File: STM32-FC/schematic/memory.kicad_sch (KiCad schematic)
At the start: 6 parts, among them J4 TF-06A, U6 W25X40CLUXIG

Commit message: v2.0.0 beta init
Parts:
- J4: footprint TF-06A:TF06A -> TF06A
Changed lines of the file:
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@@
 			)
 		)
-		(property "Footprint" "TF-06A:TF06A"
+		(property "Footprint" "TF06A"
 			(at 177.8 127.94 0)
 			(effects

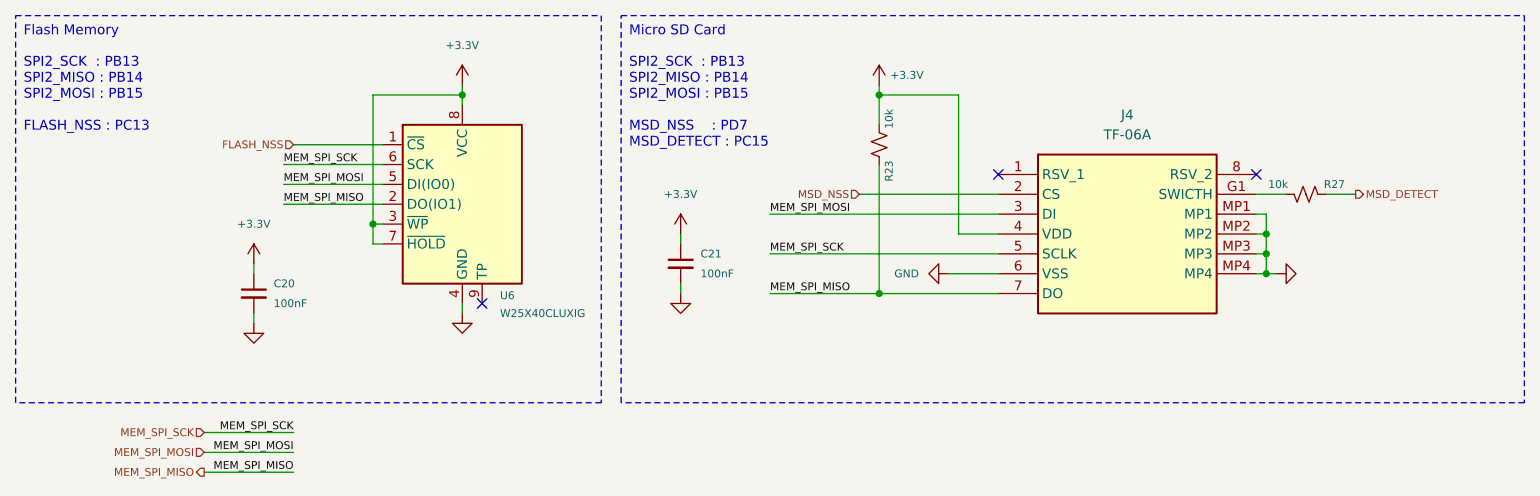
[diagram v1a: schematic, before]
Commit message: add basic circuit stm32f7
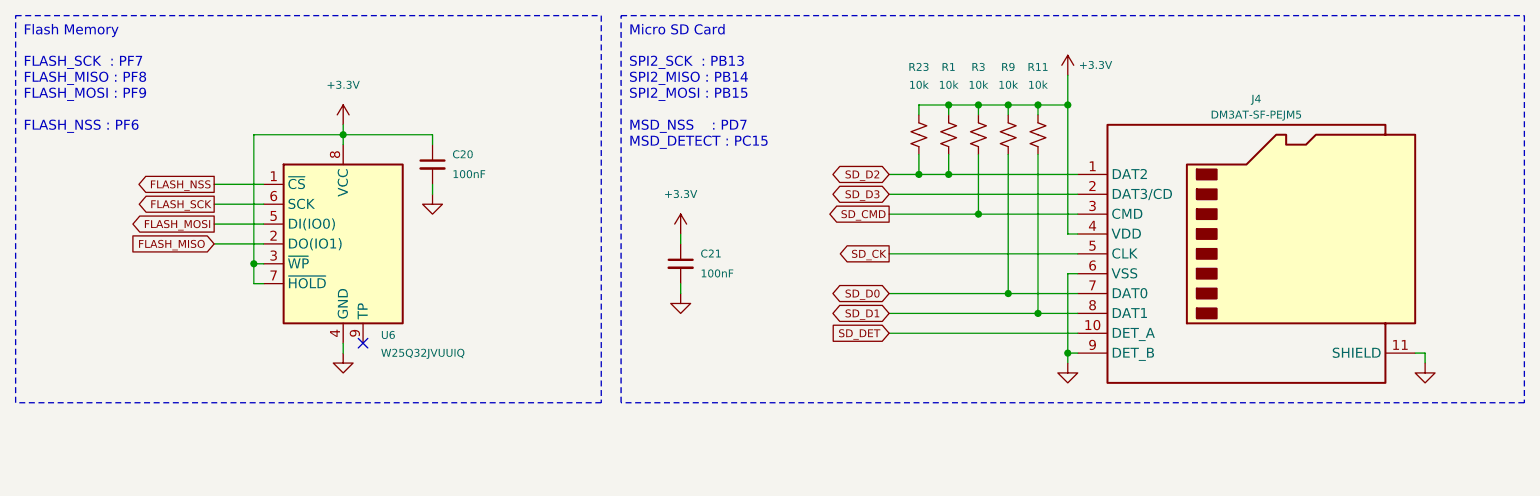
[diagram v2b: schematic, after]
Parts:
- removed J4: TF-06A, TF06A, symbol TF-06A:TF-06A
- removed R27: 10k, Resistor_SMD:R_0402_1005Metric, symbol Device:R_Small_US
- added J4: DM3AT-SF-PEJM5, Connector_Card:microSD_HC_Hirose_DM3AT-SF-PEJM5, symbol Connector:Micro_SD_Card_Det2
- added R1, R11, R3, R9: 10k, Resistor_SMD:R_0402_1005Metric, symbol Device:R_Small_US
- U6: value W25X40CLUXIG -> W25Q32JVUUIQ; symbol W25X40CLUX:W25X40CLUX -> W25X40CLUX:W25Q32JVUUIQ
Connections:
- net +3.3V: now also J4.4 (VDD), R1.1, R11.1, R3.1, R9.1
- net GND: now also J4.11 (SHIELD), J4.6 (VSS), J4.9 (DET_B)
- net MEM_SPI_MISO renamed FLASH_MISO
- net FLASH_MISO: no longer R23.2
- net MEM_SPI_MOSI renamed FLASH_MOSI
- net MEM_SPI_SCK renamed FLASH_SCK
- new net SD_CK: J4.5 (CLK)
- new net SD_CMD: J4.3 (CMD), R3.2
- new net SD_D0: J4.7 (DAT0), R9.2
- new net SD_D1: J4.8 (DAT1), R11.2
- new net SD_D2: J4.1 (DAT2), R1.2, R23.2
- new net SD_D3: J4.2 (DAT3/CD)
- new net SD_DET: J4.10 (DET_A)
- no-connect marks 3 -> 1
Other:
- note added: "FLASH_SCK : PF7 FLASH_MISO : PF8 FLASH_MOSI : PF9 FLASH_NSS : PF6"
- note removed: "SPI2_SCK : PB13 SPI2_MISO : PB14 SPI2_MOSI : PB15 FLASH_NSS : PC13"
- moved on the sheet: C20, R23, U6

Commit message: ERC passed
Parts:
- renumbered C20 to C47, C21 to C48, R23 to R14, R1 to R15, R3 to R16, R9 to R17, R11 to R18, U6 to U10
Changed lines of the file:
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@@
 		(on_board yes)
 		(dnp no)
-		(property "Reference" "R11"
+		(property "Reference" "R18"
 			(at 153.67 19.304 0)
 			(effects
@@
 			(project "STM32-FC"
 				(path "/8d4cc317-3933-4aa6-844b-8c5c635e89c7/3e7c6c79-bc31-4cc9-af6a-d0a28245a7b2"
-					(reference "R11")
+					(reference "R18")
 					(unit 1)
 				)
@@
 		(on_board yes)
 		(dnp no)
-		(property "Reference" "R9"
+		(property "Reference" "R17"
 			(at 149.86 19.304 0)
 			(effects
@@
 			(project "STM32-FC"
 				(path "/8d4cc317-3933-4aa6-844b-8c5c635e89c7/3e7c6c79-bc31-4cc9-af6a-d0a28245a7b2"
-					(reference "R9")
+					(reference "R17")
 					(unit 1)
 				)
@@
 		(on_board yes)
 		(dnp no)
-		(property "Reference" "R3"
+		(property "Reference" "R16"
 			(at 146.05 19.304 0)
 			(effects
@@
 			(project "STM32-FC"
 				(path "/8d4cc317-3933-4aa6-844b-8c5c635e89c7/3e7c6c79-bc31-4cc9-af6a-d0a28245a7b2"
-					(reference "R3")
+					(reference "R16")
 					(unit 1)
 				)
@@
 		(dnp no)
 		(fields_autoplaced yes)
-		(property "Reference" "#PWR059"
+		(property "Reference" "#PWR083"
 			(at 107.95 54.61 0)
 			(effects
@@
 			(project ""
 				(path "/8d4cc317-3933-4aa6-844b-8c5c635e89c7/3e7c6c79-bc31-4cc9-af6a-d0a28245a7b2"
-					(reference "#PWR059")
+					(reference "#PWR083")
 					(unit 1)
 				)
@@
 		(dnp no)
 		(fields_autoplaced yes)
-		(property "Reference" "#PWR055"
+		(property "Reference" "#PWR081"
 			(at 76.2 41.91 0)
 			(effects
@@
 			(project ""
 				(path "/8d4cc317-3933-4aa6-844b-8c5c635e89c7/3e7c6c79-bc31-4cc9-af6a-d0a28245a7b2"
-					(reference "#PWR055")
+					(reference "#PWR081")
 					(unit 1)
 				)
@@
 		(on_board yes)
 		(dnp no)
-		(property "Reference" "R23"
+		(property "Reference" "R14"
 			(at 138.43 19.304 0)
 			(effects
@@
 			(project "STM32-FC"
 				(path "/8d4cc317-3933-4aa6-844b-8c5c635e89c7/3e7c6c79-bc31-4cc9-af6a-d0a28245a7b2"
-					(reference "R23")
+					(reference "R14")
 					(unit 1)
 				)
@@
 		(dnp no)
 		(fields_autoplaced yes)
-		(property "Reference" "#PWR056"
+		(property "Reference" "#PWR079"
 			(at 64.77 30.48 0)
 			(effects
@@
 			(project ""
 				(path "/8d4cc317-3933-4aa6-844b-8c5c635e89c7/3e7c6c79-bc31-4cc9-af6a-d0a28245a7b2"
-					(reference "#PWR056")
+					(reference "#PWR079")
 					(unit 1)
 				)
@@
 		(on_board yes)
 		(dnp no)
-		(property "Reference" "R1"
+		(property "Reference" "R15"
 			(at 142.24 19.304 0)
 			(effects
@@
 			(project "STM32-FC"
 				(path "/8d4cc317-3933-4aa6-844b-8c5c635e89c7/3e7c6c79-bc31-4cc9-af6a-d0a28245a7b2"
-					(reference "R1")
+					(reference "R15")
 					(unit 1)
 				)
@@
 		(dnp no)
 		(fields_autoplaced yes)
-		(property "Reference" "#PWR061"
+		(property "Reference" "#PWR085"
 			(at 157.48 63.5 0)
 			(effects
@@
 			(project "STM32-FC"
 				(path "/8d4cc317-3933-4aa6-844b-8c5c635e89c7/3e7c6c79-bc31-4cc9-af6a-d0a28245a7b2"
-					(reference "#PWR061")
+					(reference "#PWR085")
 					(unit 1)
 				)
@@
 		(on_board yes)
 		(dnp no)
-		(property "Reference" "C20"
+		(property "Reference" "C47"
 			(at 78.74 30.48 0)
 			(effects
@@
 			(project "STM32-FC"
 				(path "/8d4cc317-3933-4aa6-844b-8c5c635e89c7/3e7c6c79-bc31-4cc9-af6a-d0a28245a7b2"
-					(reference "C20")
+					(reference "C47")
 					(unit 1)
 				)
@@
 		(on_board yes)
 		(dnp no)
-		(property "Reference" "C21"
+		(property "Reference" "C48"
 			(at 110.49 43.18 0)
 			(effects
@@
 			(project "STM32-FC"
 				(path "/8d4cc317-3933-4aa6-844b-8c5c635e89c7/3e7c6c79-bc31-4cc9-af6a-d0a28245a7b2"
-					(reference "C21")
+					(reference "C48")
 					(unit 1)
 				)
@@
 		(dnp no)
 		(fields_autoplaced yes)
-		(property "Reference" "#PWR058"
+		(property "Reference" "#PWR082"
 			(at 107.95 44.45 0)
 			(effects
@@
 			(project ""
 				(path "/8d4cc317-3933-4aa6-844b-8c5c635e89c7/3e7c6c79-bc31-4cc9-af6a-d0a28245a7b2"
-					(reference "#PWR058")
+					(reference "#PWR082")
 					(unit 1)
 				)
@@
 		(dnp no)
 		(fields_autoplaced yes)
-		(property "Reference" "#PWR05"
+		(property "Reference" "#PWR086"
 			(at 203.2 63.5 0)
 			(effects
@@
 			(project "STM32-FC"
 				(path "/8d4cc317-3933-4aa6-844b-8c5c635e89c7/3e7c6c79-bc31-4cc9-af6a-d0a28245a7b2"
-					(reference "#PWR05")
+					(reference "#PWR086")
 					(unit 1)
 				)
@@
 		(dnp no)
 		(fields_autoplaced yes)
-		(property "Reference" "#PWR057"
+		(property "Reference" "#PWR080"
 			(at 64.77 62.23 0)
 			(effects
@@
 			(project ""
 				(path "/8d4cc317-3933-4aa6-844b-8c5c635e89c7/3e7c6c79-bc31-4cc9-af6a-d0a28245a7b2"
-					(reference "#PWR057")
+					(reference "#PWR080")
 					(unit 1)
 				)
@@
 		(on_board yes)
 		(dnp no)
-		(property "Reference" "U6"
+		(property "Reference" "U10"
 			(at 69.596 53.594 0)
 			(effects
@@
 			(project "STM32-FC"
 				(path "/8d4cc317-3933-4aa6-844b-8c5c635e89c7/3e7c6c79-bc31-4cc9-af6a-d0a28245a7b2"
-					(reference "U6")
+					(reference "U10")
 					(unit 1)
 				)
@@
 		(on_board yes)
 		(dnp no)
-		(property "Reference" "#PWR060"
+		(property "Reference" "#PWR084"
 			(at 157.48 24.13 0)
 			(effects
@@
 			(project "STM32-FC"
 				(path "/8d4cc317-3933-4aa6-844b-8c5c635e89c7/3e7c6c79-bc31-4cc9-af6a-d0a28245a7b2"
-					(reference "#PWR060")
+					(reference "#PWR084")
 					(unit 1)
 				)
